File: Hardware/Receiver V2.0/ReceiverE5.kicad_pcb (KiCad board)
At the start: 4 copper layers, 50 x 35.5 mm, 44 parts, among them J1 KBUS, J2 AVR-PDI-6A, J3 CONN_01X08, J4 CONN_01X06, J5 CONN_01X06, J6 CONN_01X04, J7 CONN_01X04, SW1 SW_SPST, U1 ATXMEGA32E5-A, U2 LM2731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

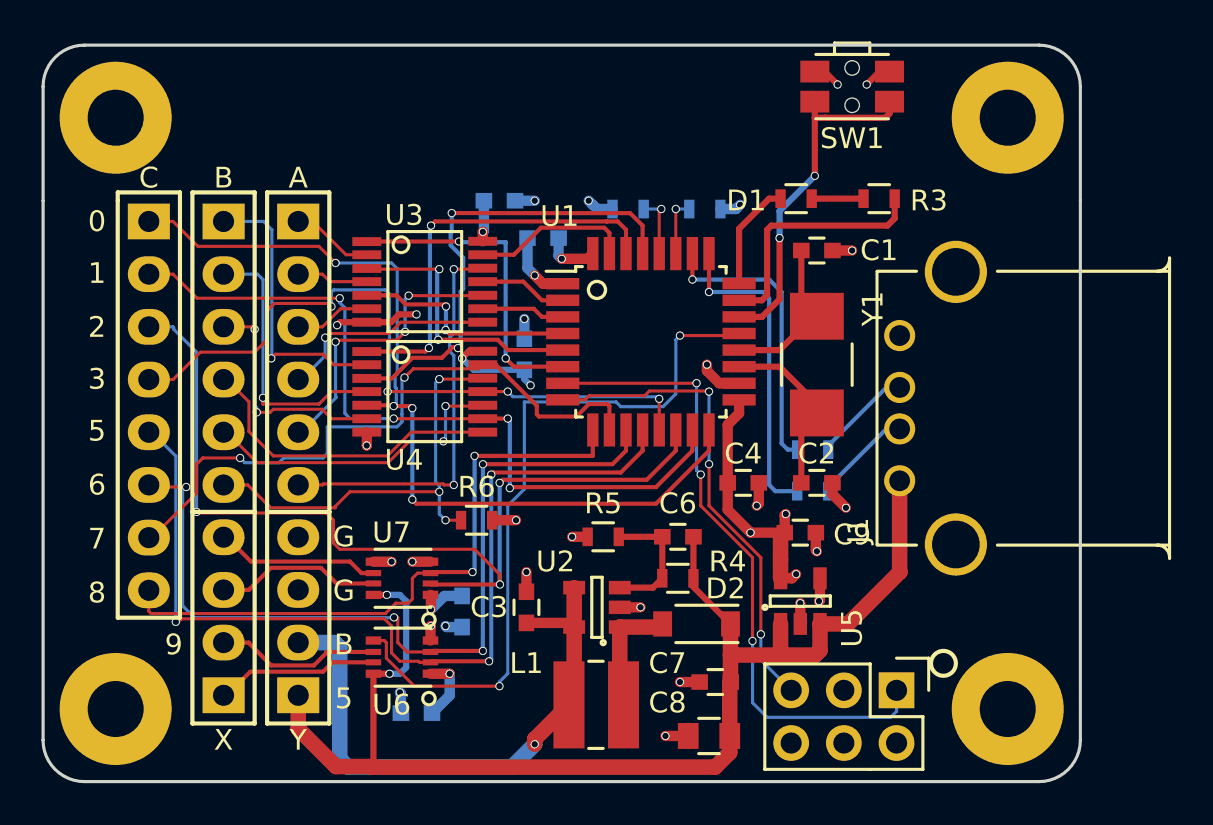
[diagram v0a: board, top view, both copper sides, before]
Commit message: Widened board, added button
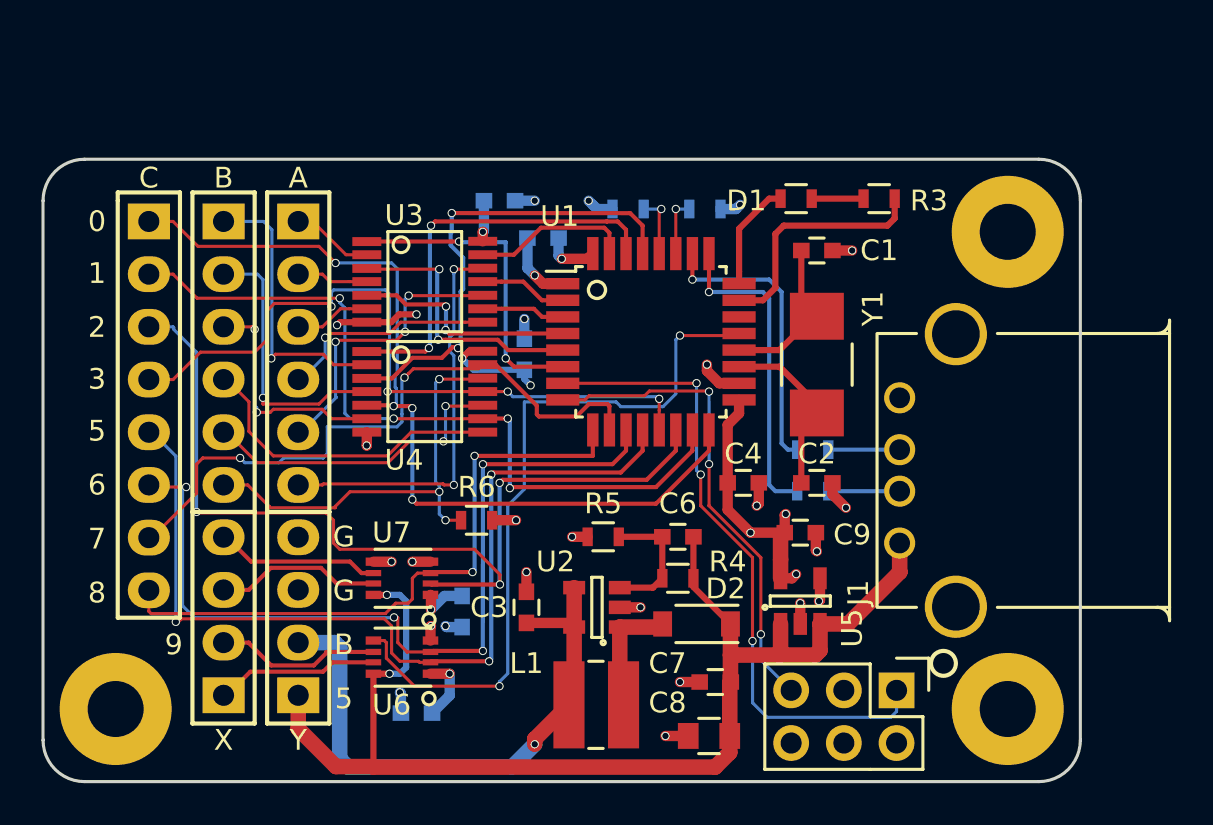
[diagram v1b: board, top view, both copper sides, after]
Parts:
- removed the REF** at (70.5, 61.0)
- removed SW1: SW_SPST, Buttons_Switches_SMD:SW_SPST_EVQP7C
- moved REF** 5.50 mm to (113.5, 66.5)
- moved J1 3.00 mm to (111.0, 78.0)
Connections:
- U1 pad 22: Net-(SW1-Pad1) -> (no net)
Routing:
- net Net-(SW1-Pad1): track 16.8 -> 0.00 mm, vias 2 -> 0
- net +5V: track 62.3 -> 59.3 mm
- net GND: track 32.9 -> 30.2 mm, vias 27 -> 25
- net Net-(J1-Pad3): track 4.80 -> 3.44 mm
- net Net-(J1-Pad2): track 4.80 -> 3.44 mm
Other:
- board size 50 x 35.5 mm -> 50 x 30 mm
